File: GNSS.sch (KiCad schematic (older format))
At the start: 3 parts

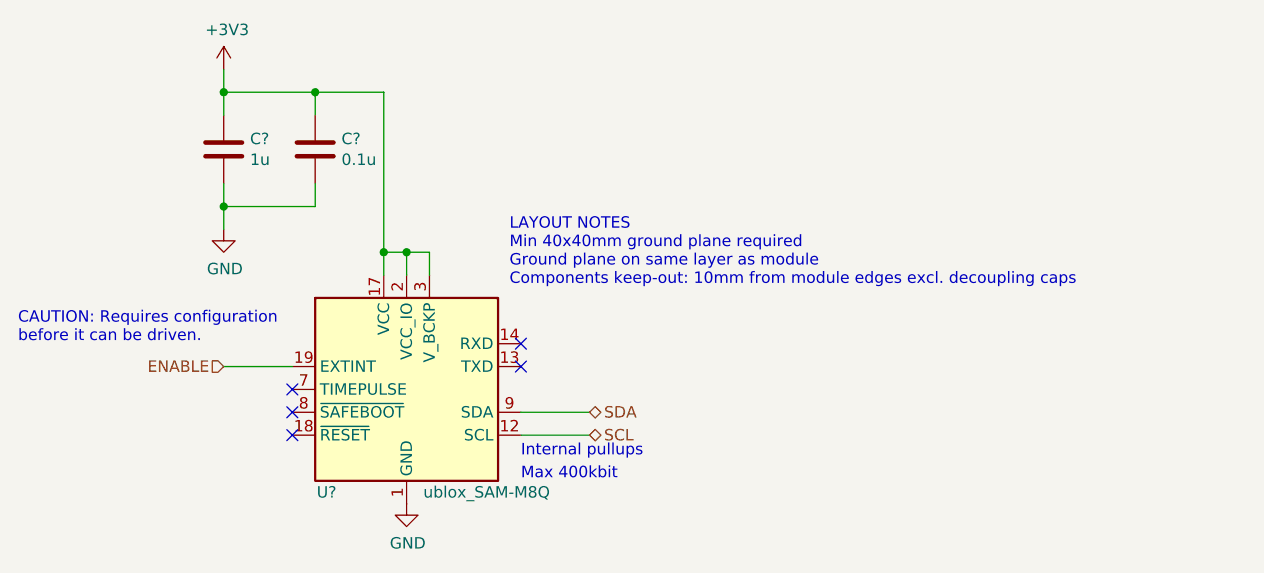
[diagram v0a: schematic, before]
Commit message: Change BME280 out for connector
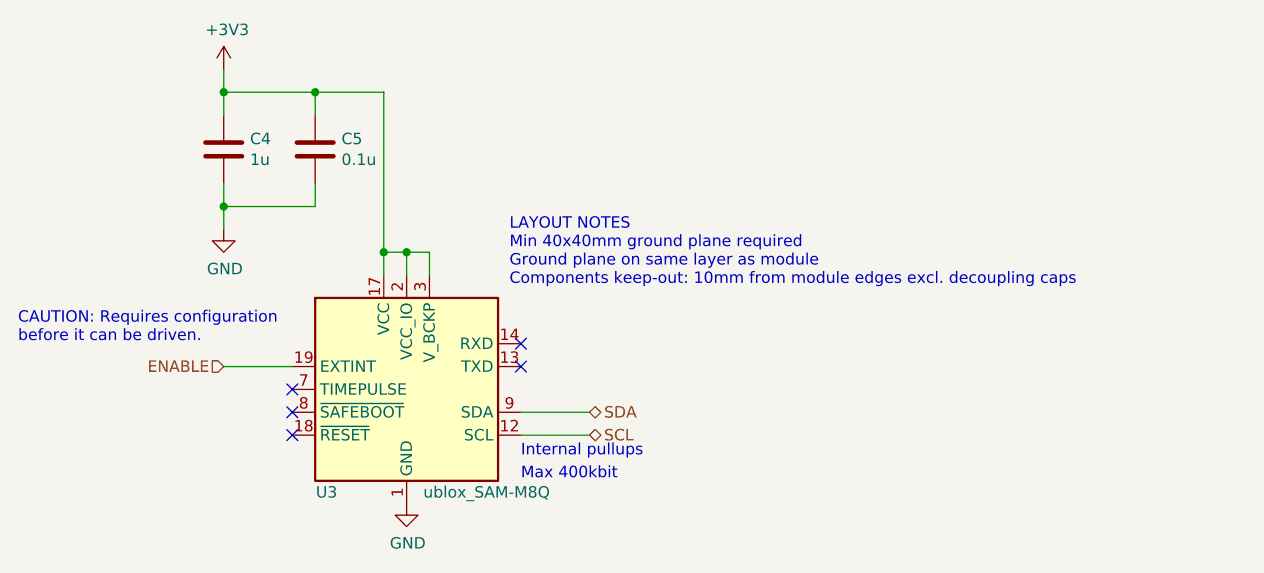
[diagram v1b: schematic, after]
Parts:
- gave numbers to parts that had none: 3
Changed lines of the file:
@@
 $EndDescr
 $Comp
-L RF_GPS:ublox_SAM-M8Q U?
+L RF_GPS:ublox_SAM-M8Q U3
 U 1 1 60A3F723
 P 4900 4000
-F 0 "U?" H 4550 3550 50  0000 C CNN
+F 0 "U3" H 4550 3550 50  0000 C CNN
 F 1 "ublox_SAM-M8Q" H 5250 3550 50  0000 C CNN
 F 2 "RF_GPS:ublox_SAM-M8Q" H 5400 3550 50  0001 C CNN
@@
 Connection ~ 4900 3400
 $Comp
-L power:GND #PWR?
+L power:GND #PWR027
 U 1 1 60A436D0
 P 4900 4500
-F 0 "#PWR?" H 4900 4250 50  0001 C CNN
+F 0 "#PWR027" H 4900 4250 50  0001 C CNN
 F 1 "GND" H 4905 4327 50  0000 C CNN
 F 2 "" H 4900 4500 50  0001 C CNN
@@
 	4100 3200 4100 3300
 $Comp
-L power:GND #PWR?
+L power:GND #PWR026
 U 1 1 60A4A74D
 P 4100 3300
-F 0 "#PWR?" H 4100 3050 50  0001 C CNN
+F 0 "#PWR026" H 4100 3050 50  0001 C CNN
 F 1 "GND" H 4105 3127 50  0000 C CNN
 F 2 "" H 4100 3300 50  0001 C CNN
@@
 	4100 2600 4100 2700
 $Comp
-L power:+3V3 #PWR?
+L power:+3V3 #PWR025
 U 1 1 60A4A756
 P 4100 2600
-F 0 "#PWR?" H 4100 2450 50  0001 C CNN
+F 0 "#PWR025" H 4100 2450 50  0001 C CNN
 F 1 "+3V3" H 4115 2773 50  0000 C CNN
 F 2 "" H 4100 2600 50  0001 C CNN
@@
 	4100 3100 4100 3200
 $Comp
-L Device:C C?
+L Device:C C5
 U 1 1 60A4A761
 P 4500 2950
-F 0 "C?" H 4615 2996 50  0000 L CNN
+F 0 "C5" H 4615 2996 50  0000 L CNN
 F 1 "0.1u" H 4615 2905 50  0000 L CNN
 F 2 "" H 4538 2800 50  0001 C CNN
@@
 $EndComp
 $Comp
-L Device:C C?
+L Device:C C4
 U 1 1 60A4A767
 P 4100 2950
-F 0 "C?" H 4215 2996 50  0000 L CNN
+F 0 "C4" H 4215 2996 50  0000 L CNN
 F 1 "1u" H 4215 2905 50  0000 L CNN
 F 2 "" H 4138 2800 50  0001 C CNN

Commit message: Begin assigning footprints
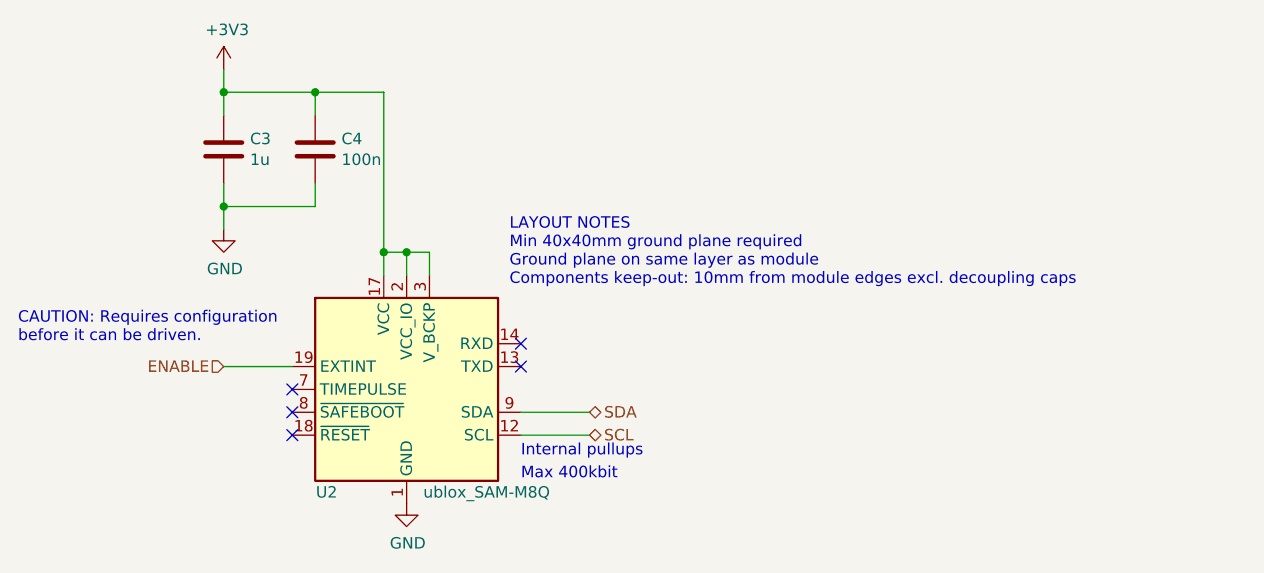
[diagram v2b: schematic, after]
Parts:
- C3: renamed from C4; footprint (none) -> Capacitor_SMD:C_0603_1608Metric; LCSC (none) -> C15849
- C4: renamed from C5; value 0.1u -> 100n; footprint (none) -> Capacitor_SMD:C_0603_1608Metric; LCSC (none) -> C14663
- renumbered U3 to U2
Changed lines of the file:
@@
 $EndDescr
 $Comp
-L RF_GPS:ublox_SAM-M8Q U3
+L RF_GPS:ublox_SAM-M8Q U2
 U 1 1 60A3F723
 P 4900 4000
-F 0 "U3" H 4550 3550 50  0000 C CNN
+F 0 "U2" H 4550 3550 50  0000 C CNN
 F 1 "ublox_SAM-M8Q" H 5250 3550 50  0000 C CNN
 F 2 "RF_GPS:ublox_SAM-M8Q" H 5400 3550 50  0001 C CNN
@@
 Connection ~ 4900 3400
 $Comp
-L power:GND #PWR027
+L power:GND #PWR025
 U 1 1 60A436D0
 P 4900 4500
-F 0 "#PWR027" H 4900 4250 50  0001 C CNN
+F 0 "#PWR025" H 4900 4250 50  0001 C CNN
 F 1 "GND" H 4905 4327 50  0000 C CNN
 F 2 "" H 4900 4500 50  0001 C CNN
@@
 	4100 3200 4100 3300
 $Comp
-L power:GND #PWR026
+L power:GND #PWR024
 U 1 1 60A4A74D
 P 4100 3300
-F 0 "#PWR026" H 4100 3050 50  0001 C CNN
+F 0 "#PWR024" H 4100 3050 50  0001 C CNN
 F 1 "GND" H 4105 3127 50  0000 C CNN
 F 2 "" H 4100 3300 50  0001 C CNN
@@
 	4100 2600 4100 2700
 $Comp
-L power:+3V3 #PWR025
+L power:+3V3 #PWR023
 U 1 1 60A4A756
 P 4100 2600
-F 0 "#PWR025" H 4100 2450 50  0001 C CNN
+F 0 "#PWR023" H 4100 2450 50  0001 C CNN
 F 1 "+3V3" H 4115 2773 50  0000 C CNN
 F 2 "" H 4100 2600 50  0001 C CNN
@@
 	4100 3100 4100 3200
 $Comp
-L Device:C C5
+L Device:C C4
 U 1 1 60A4A761
 P 4500 2950
-F 0 "C5" H 4615 2996 50  0000 L CNN
-F 1 "0.1u" H 4615 2905 50  0000 L CNN
-F 2 "" H 4538 2800 50  0001 C CNN
+F 0 "C4" H 4615 2996 50  0000 L CNN
+F 1 "100n" H 4615 2905 50  0000 L CNN
+F 2 "Capacitor_SMD:C_0603_1608Metric" H 4538 2800 50  0001 C CNN
 F 3 "~" H 4500 2950 50  0001 C CNN
+F 4 "C14663" H 4500 2950 50  0001 C CNN "LCSC"
 	1    4500 2950
 	1    0    0    -1
 $EndComp
 $Comp
-L Device:C C4
+L Device:C C3
 U 1 1 60A4A767
 P 4100 2950
-F 0 "C4" H 4215 2996 50  0000 L CNN
+F 0 "C3" H 4215 2996 50  0000 L CNN
 F 1 "1u" H 4215 2905 50  0000 L CNN
-F 2 "" H 4138 2800 50  0001 C CNN
+F 2 "Capacitor_SMD:C_0603_1608Metric" H 4138 2800 50  0001 C CNN
 F 3 "~" H 4100 2950 50  0001 C CNN
+F 4 "C15849" H 4100 2950 50  0001 C CNN "LCSC"
 	1    4100 2950
 	1    0    0    -1
